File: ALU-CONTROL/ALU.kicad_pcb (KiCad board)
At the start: 4 copper layers, 148.9 x 76.4 mm, 64 parts, among them J1 Conn_01x02, J2 Conn_01x08, J3 Conn_01x08, J4 Conn_01x08, J5 Conn_01x04, J6 Conn_01x08, J7 Conn_01x02, U1 74LS08, U10 74LS245, U2 74LS245, U3 74LS08, U4 74LS32, U5 74LS86, U6 74LS245, U7 74LS32, U8 74LS245, U9 74LS86

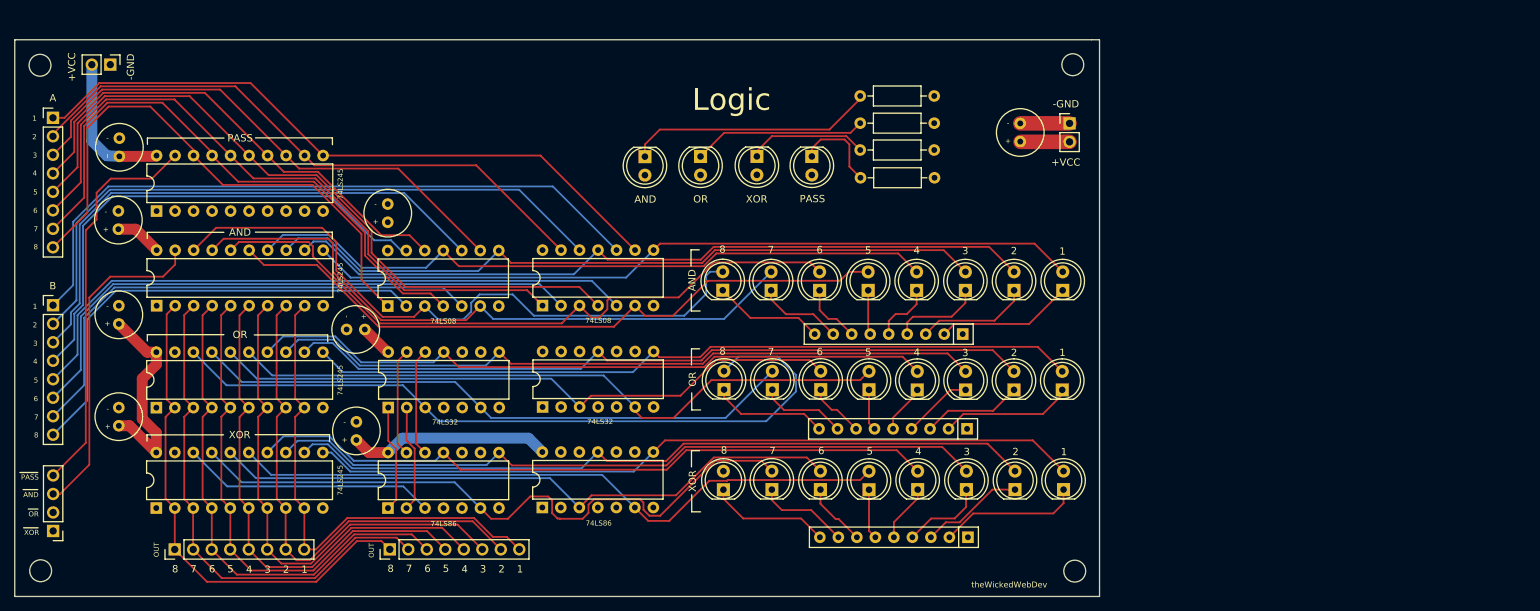
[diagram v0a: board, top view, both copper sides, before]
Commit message: Adding Programmable RAM Module
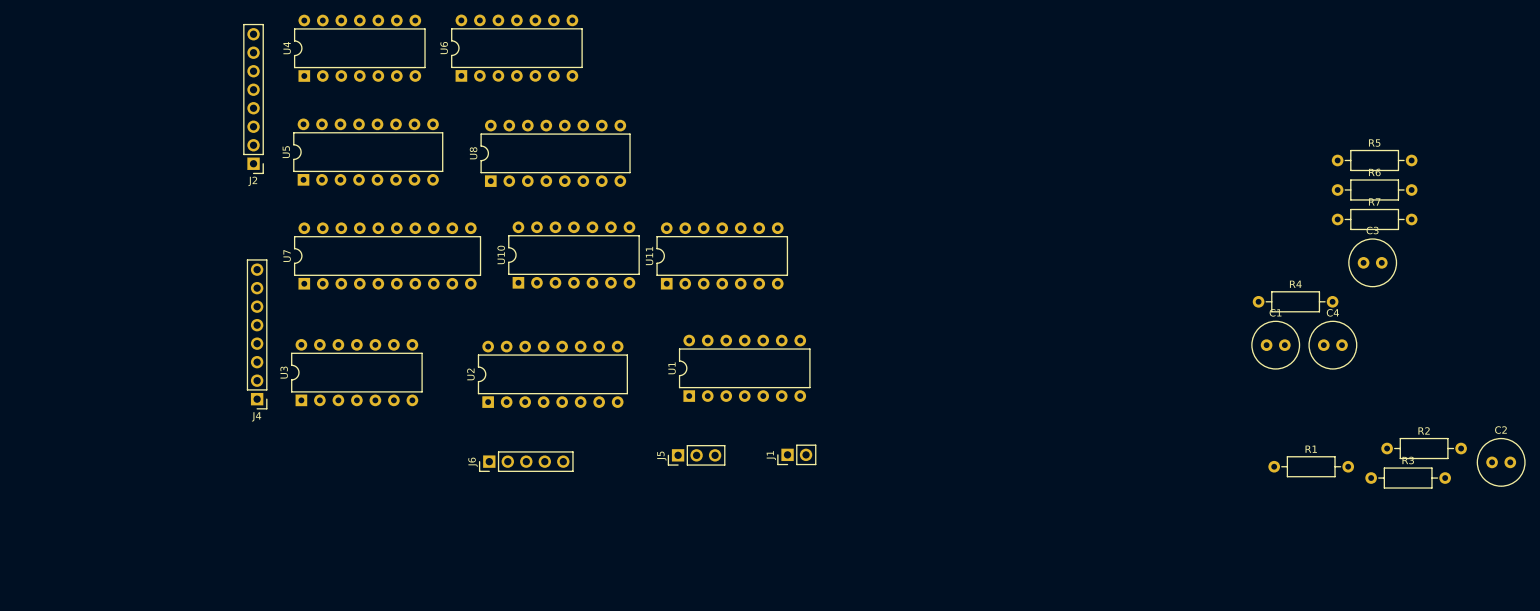
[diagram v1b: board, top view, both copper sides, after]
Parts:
- removed C5, C6, C7, C8: CP1, Capacitor_THT:C_Radial_D6.3mm_H11.0mm_P2.50mm
- removed D1, D10, D11, D12, D13, D14, D15, D16, D17, D18, D19, D2, D20, D21, D22, D23, D24, D25, D26, D27, D28, D3, D4, D5, D6, D7, D8, D9: LED, LED_THT:LED_D5.0mm
- removed J3: Conn_01x08, Connector_PinHeader_2.54mm:PinHeader_1x08_P2.54mm_Vertical
- removed J7: Conn_01x02, Connector_PinHeader_2.54mm:PinHeader_1x02_P2.54mm_Vertical
- removed REF** (x4): MountingHole_3mm, MountingHole:MountingHole_3mm
- removed RN1, RN2, RN3: R_Network08_US, Resistor_THT:R_Array_SIP9
- removed U9: 74LS86, Package_DIP:DIP-14_W7.62mm
- added R5: R_US, Resistor_THT:R_Axial_DIN0207_L6.3mm_D2.5mm_P10.16mm_Horizontal, F.Cu at (247.3, 44.4)
- added R6: R_US, Resistor_THT:R_Axial_DIN0207_L6.3mm_D2.5mm_P10.16mm_Horizontal, F.Cu at (247.3, 48.4)
- added R7: R_US, Resistor_THT:R_Axial_DIN0207_L6.3mm_D2.5mm_P10.16mm_Horizontal, F.Cu at (247.3, 52.5)
- added U11: 74LS08, Package_DIP:DIP-14_W7.62mm, F.Cu at (155.2, 61.3)
- J5: value Conn_01x04 -> Conn_01x03; footprint Connector_PinHeader_2.54mm:PinHeader_1x04_P2.54mm_Vertical -> Connector_PinHeader_2.54mm:PinHeader_1x03_P2.54mm_Vertical
- J6: value Conn_01x08 -> Conn_01x05; footprint Connector_PinHeader_2.54mm:PinHeader_1x08_P2.54mm_Vertical -> Connector_PinHeader_2.54mm:PinHeader_1x05_P2.54mm_Vertical
- R1, R2, R3, R4: value R_Small_US -> R_US
- U10: value 74LS245 -> 74LS02; footprint Package_DIP:DIP-20_W7.62mm -> Package_DIP:DIP-14_W7.62mm
- U2: value 74LS245 -> 74LS138; footprint Package_DIP:DIP-20_W7.62mm -> Package_DIP:DIP-16_W7.62mm
- U4: value 74LS32 -> 74LS04
- U5: value 74LS86 -> 74LS157; footprint Package_DIP:DIP-14_W7.62mm -> Package_DIP:DIP-16_W7.62mm
- U6: value 74LS245 -> 74LS04; footprint Package_DIP:DIP-20_W7.62mm -> Package_DIP:DIP-14_W7.62mm
- U7: value 74LS32 -> 74LS245; footprint Package_DIP:DIP-14_W7.62mm -> Package_DIP:DIP-20_W7.62mm
- U8: value 74LS245 -> 74LS157; footprint Package_DIP:DIP-20_W7.62mm -> Package_DIP:DIP-16_W7.62mm
- moved C2 189.5 mm to (268.5, 85.8), turned to 0 degrees
- moved C3 172.3 mm to (250.8, 58.4), turned to 0 degrees
- moved C4 166.2 mm to (245.4, 69.7), turned to 0 degrees
- moved R3 87.6 mm to (251.9, 87.9)
- moved J5 86.4 mm to (156.7, 84.8), turned to 90 degrees
- moved R2 85.0 mm to (254.1, 83.9)
- moved R1 71.6 mm to (238.6, 86.4)
- moved U8 64.2 mm to (131.0, 47.2)
- moved U6 61.9 mm to (127.0, 32.7)
- moved J1 59.7 mm to (171.7, 84.8), turned to 90 degrees
- moved R4 57.2 mm to (236.4, 63.8)
- moved U10 50.6 mm to (134.8, 61.1)
- moved U2 47.4 mm to (130.6, 77.5)
- moved U4 47.0 mm to (105.4, 32.8)
- moved U5 46.5 mm to (105.3, 47.0)
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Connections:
- J2 pad 1: A1 -> /Y8
- J2 pad 2: A2 -> /Y7
- J2 pad 3: A3 -> /Y6
- J2 pad 4: A4 -> /Y5
- J2 pad 5: A5 -> /Y4
- J2 pad 6: A6 -> /Y3
- J2 pad 7: A7 -> /Y2
- J2 pad 8: A8 -> /Y1
- J4 pad 1: /Y8 -> /ALU_OUT1
- J4 pad 2: /Y7 -> /ALU_OUT2
- J4 pad 3: /Y6 -> /ALU_OUT3
- J4 pad 4: /Y5 -> /ALU_OUT4
- J4 pad 5: /Y4 -> /ALU_OUT5
- J4 pad 6: /Y3 -> /ALU_OUT6
- J4 pad 7: /Y2 -> /ALU_OUT7
- J4 pad 8: /Y1 -> /ALU_OUT8
- J5 pad 1: /XOR_OUT -> /CARRY_OUT
- J5 pad 2: /OR_OUT -> /NEG
- J5 pad 3: /AND_OUT -> /ZE
- J6 pad 1: /Y8 -> /F0
- J6 pad 2: /Y7 -> /F1
- J6 pad 3: /Y6 -> /F2
- J6 pad 4: /Y5 -> /INVERT
- J6 pad 5: /Y4 -> /ALU_EN
- R1 pad 1: Net-(D25-Pad1) -> GND
- R1 pad 2: GND -> Net-(R1-Pad2)
- R2 pad 1: Net-(D26-Pad1) -> GND
- R2 pad 2: GND -> Net-(R2-Pad2)
- R3 pad 1: Net-(D27-Pad1) -> GND
- R3 pad 2: GND -> Net-(R3-Pad2)
- R4 pad 1: Net-(D28-Pad1) -> GND
- R4 pad 2: GND -> Net-(R4-Pad2)
- U1 pad 1: A8 -> /SUB
- U1 pad 10: B3 -> Net-(R1-Pad2)
- U1 pad 11: Net-(D5-Pad2) -> Net-(U1-Pad11)
- U1 pad 12: A4 -> Net-(U1-Pad12)
- U1 pad 13: B4 -> Net-(U1-Pad13)
- U1 pad 2: B8 -> /SUM_HIGH_BIT
- U1 pad 3: Net-(D1-Pad2) -> /NEG
- U1 pad 4: A7 -> /SUB
- U1 pad 5: B7 -> /EQ
- U1 pad 6: Net-(D2-Pad2) -> /ZE
- U1 pad 8: Net-(D6-Pad2) -> Net-(U1-Pad8)
- U1 pad 9: A3 -> Net-(R2-Pad2)
- U10 pad 1: GND -> Net-(U10-Pad1)
- U10 pad 10: GND -> Net-(U10-Pad10)
- U10 pad 11: A1 -> /SUM1
- U10 pad 12: A2 -> /SUM2
- U10 pad 13: A3 -> Net-(U10-Pad13)
- U10 pad 14: A4 -> VCC
- U10 pad 2: /Y8 -> /SUM7
- U10 pad 3: /Y7 -> /SUM8
- U10 pad 4: /Y6 -> Net-(U10-Pad4)
- U10 pad 5: /Y5 -> /SUM5
- U10 pad 6: /Y4 -> /SUM6
- U10 pad 7: /Y3 -> GND
- U10 pad 8: /Y2 -> /SUM3
- U10 pad 9: /Y1 -> /SUM4
- U2 pad 1: GND -> /F0
- U2 pad 10: GND -> /SHL
- U2 pad 11: Net-(D8-Pad2) -> /XOR_OUT
- U2 pad 12: Net-(D7-Pad2) -> /OR_OUT
- U2 pad 13: Net-(D6-Pad2) -> /AND_OUT
- U2 pad 14: Net-(D5-Pad2) -> Net-(U2-Pad14)
- U2 pad 15: Net-(D4-Pad2) -> Net-(U2-Pad15)
- U2 pad 16: Net-(D3-Pad2) -> VCC
- U2 pad 2: /Y8 -> /F1
- U2 pad 3: /Y7 -> /F2
- U2 pad 4: /Y6 -> GND
- U2 pad 5: /Y5 -> GND
- U2 pad 6: /Y4 -> VCC
- U2 pad 7: /Y3 -> /PASS
- U2 pad 8: /Y2 -> GND
- U2 pad 9: /Y1 -> /SHR
- U3 pad 1: A6 -> Net-(U2-Pad14)
- U3 pad 10: B1 -> Net-(U11-Pad3)
- U3 pad 11: Net-(D7-Pad2) -> Net-(U3-Pad11)
- U3 pad 12: B2 -> Net-(R7-Pad2)
- U3 pad 13: A2 -> Net-(R6-Pad2)
- U3 pad 2: B6 -> Net-(U2-Pad15)
- U3 pad 3: Net-(D3-Pad2) -> /SUM_OUT
- U3 pad 4: A5 -> (no net)
- U3 pad 5: B5 -> (no net)
- U3 pad 6: Net-(D4-Pad2) -> (no net)
- U3 pad 8: Net-(D8-Pad2) -> /EQ
- U3 pad 9: A1 -> Net-(U11-Pad6)
- U4 pad 1: A8 -> /Y8
- U4 pad 10: B3 -> Net-(U4-Pad10)
- U4 pad 11: Net-(D13-Pad2) -> /Y4
- U4 pad 12: A4 -> Net-(U4-Pad12)
- U4 pad 13: B4 -> /Y3
- U4 pad 2: B8 -> Net-(U4-Pad2)
- U4 pad 3: Net-(U4-Pad3) -> /Y7
- U4 pad 4: A7 -> Net-(U4-Pad4)
- U4 pad 5: B7 -> Net-(U2-Pad14)
- U4 pad 6: Net-(D10-Pad2) -> /SUB
- U4 pad 8: Net-(D14-Pad2) -> Net-(U4-Pad8)
- U4 pad 9: A3 -> /Y5
- U5 pad 1: A8 -> /INVERT
- U5 pad 10: B3 -> Net-(U4-Pad4)
- U5 pad 11: Net-(D21-Pad2) -> /Y7
- U5 pad 12: A4 -> Net-(U5-Pad12)
- U5 pad 13: B4 -> Net-(U4-Pad2)
- U5 pad 14: VCC -> /Y8
- U5 pad 2: B8 -> /Y5
- U5 pad 3: Net-(D17-Pad2) -> Net-(U4-Pad8)
- U5 pad 4: A7 -> Net-(U5-Pad4)
- U5 pad 5: B7 -> /Y6
- U5 pad 6: Net-(D18-Pad2) -> Net-(U5-Pad6)
- U5 pad 7: GND -> Net-(U5-Pad7)
- U5 pad 8: Net-(D22-Pad2) -> GND
- U5 pad 9: A3 -> Net-(U5-Pad9)
- U6 pad 1: GND -> /Y2
- U6 pad 10: GND -> Net-(U6-Pad10)
- U6 pad 11: Net-(D16-Pad2) -> Net-(R4-Pad2)
- U6 pad 12: Net-(D15-Pad2) -> Net-(U6-Pad12)
- U6 pad 13: Net-(D14-Pad2) -> Net-(R5-Pad2)
- U6 pad 14: Net-(D13-Pad2) -> VCC
- U6 pad 2: /Y8 -> Net-(U6-Pad2)
- U6 pad 3: /Y7 -> /Y1
- U6 pad 4: /Y6 -> Net-(U6-Pad4)
- U6 pad 5: /Y5 -> /Y6
- U6 pad 6: /Y4 -> Net-(U5-Pad6)
- U6 pad 7: /Y3 -> GND
- U6 pad 8: /Y2 -> Net-(U6-Pad8)
- U6 pad 9: /Y1 -> Net-(R3-Pad2)
- U7 pad 1: A6 -> GND
- U7 pad 10: B1 -> GND
- U7 pad 11: Net-(D15-Pad2) -> Net-(U7-Pad11)
- U7 pad 12: B2 -> Net-(U7-Pad12)
- U7 pad 13: A2 -> Net-(U7-Pad13)
- U7 pad 14: VCC -> Net-(U7-Pad14)
- U7 pad 2: B6 -> /ALU_OUT8
- U7 pad 3: Net-(D11-Pad2) -> /ALU_OUT7
- U7 pad 4: A5 -> /ALU_OUT6
- U7 pad 5: B5 -> /ALU_OUT5
- U7 pad 6: Net-(D12-Pad2) -> /ALU_OUT4
- U7 pad 7: GND -> /ALU_OUT3
- U7 pad 8: Net-(D16-Pad2) -> /ALU_OUT2
- U7 pad 9: A1 -> /ALU_OUT1
- U8 pad 1: GND -> /INVERT
- U8 pad 10: GND -> /Y3
- U8 pad 11: Net-(D24-Pad2) -> Net-(U4-Pad12)
- U8 pad 12: Net-(D23-Pad2) -> Net-(U7-Pad14)
- U8 pad 13: Net-(D22-Pad2) -> /Y4
- U8 pad 14: Net-(D21-Pad2) -> Net-(U4-Pad10)
- U8 pad 15: Net-(D20-Pad2) -> GND
- U8 pad 16: Net-(D19-Pad2) -> VCC
- U8 pad 2: /Y8 -> Net-(U6-Pad4)
- U8 pad 3: /Y7 -> /Y1
- U8 pad 4: /Y6 -> Net-(U7-Pad11)
- U8 pad 5: /Y5 -> Net-(U6-Pad2)
- U8 pad 6: /Y4 -> /Y2
- U8 pad 7: /Y3 -> Net-(U7-Pad12)
- U8 pad 8: /Y2 -> GND
- U8 pad 9: /Y1 -> Net-(U7-Pad13)
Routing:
- net VCC: track 289.7 -> 0.00 mm
- net /PASS: track 145.9 -> 0.00 mm
- net /XOR_OUT: track 134.2 -> 0.00 mm
- net A5: track 127.3 -> 0.00 mm
- net B1: track 122.5 -> 0.00 mm
- net /OR_OUT: track 121.9 -> 0.00 mm
- net A6: track 121.5 -> 0.00 mm
- net A1: track 121.1 -> 0.00 mm
- net B2: track 119.3 -> 0.00 mm
- net /AND_OUT: track 117.7 -> 0.00 mm
- net B5: track 117.3 -> 0.00 mm
- net A2: track 111.8 -> 0.00 mm
- net B6: track 111.5 -> 0.00 mm
- net A7: track 109.9 -> 0.00 mm
- net Net-(D8-Pad2): track 106.6 -> 0.00 mm
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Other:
- board outline removed
- board text removed: "+"
- board text removed: "+VCC"
- board text removed: "-"
- board text removed: "-GND"
- board text removed: "1"
- board text removed: "2"
- board text removed: "3"
- board text removed: "4"
- board text removed: "5"
- board text removed: "6"
- board text removed: "7"
- board text removed: "74LS08"
- board text removed: "74LS245"
- board text removed: "74LS32"
- board text removed: "74LS86"
- board text removed: "8"
- board text removed: "A"
- board text removed: "AND"
- board text removed: "B"
- board text removed: "Logic"
- board text removed: "OR"
- board text removed: "OUT"
- board text removed: "PASS"
- board text removed: "XOR"
- board text removed: "theWickedWebDev"
